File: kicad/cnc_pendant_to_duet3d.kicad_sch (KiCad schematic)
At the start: 9 parts, among them J1 Conn_01x04_Male, J2 DA15_Socket_MountingHoles, U1 Sparkfun_Pro_Micro

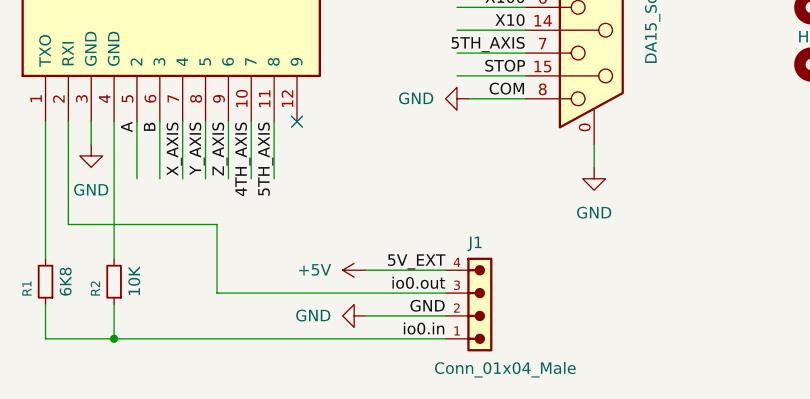
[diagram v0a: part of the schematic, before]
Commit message: Confusion over connecting to Duet and PanelDue
Change to silkscreens
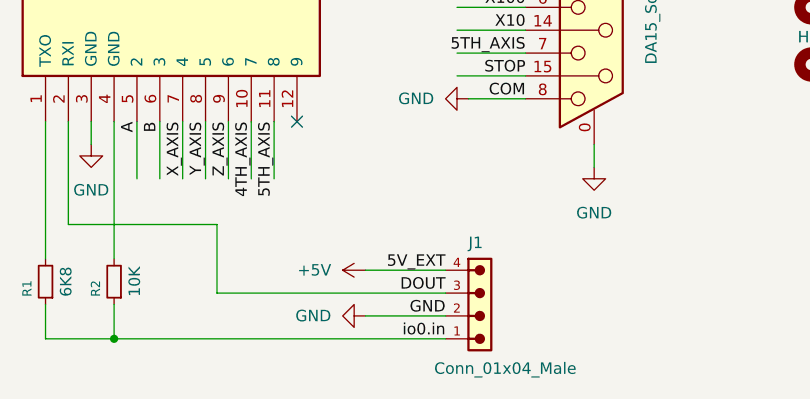
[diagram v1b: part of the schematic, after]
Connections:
- net io0.out renamed DOUT
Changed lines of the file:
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@@
 		)
 	)
-	(label "io0.out"
+	(label "DOUT"
 		(at 82.55 86.36 180)
 		(effects

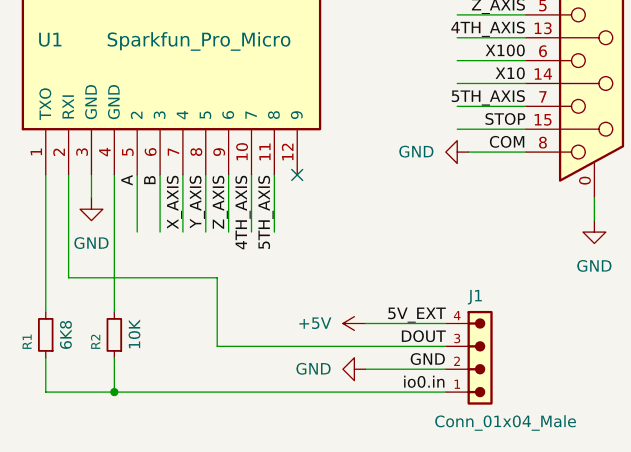
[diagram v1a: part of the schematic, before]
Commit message: 10k resistor and Arduino pin 4 to GND
PCB not updated from schematic at this point
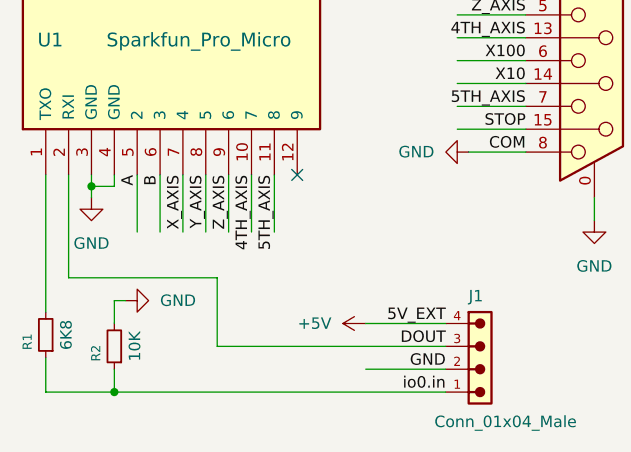
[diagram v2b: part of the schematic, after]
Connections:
- net GND: now also R2.2, U1.4 (GND)
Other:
- moved on the sheet: R2
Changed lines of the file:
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@@
+		(color 0 0 0 0)
+	)
+	(junction
+		(at 43.18 68.58)
+		(diameter 0)
 		(color 0 0 0 0)
 	)
@@
 	(wire
 		(pts
+			(xy 45.72 67.31) (xy 45.72 68.58)
+		)
+		(stroke
+			(width 0)
+			(type default)
+		)
+	)
+	(wire
+		(pts
 			(xy 151.13 54.61) (xy 151.13 57.15)
 		)
@@
 	(wire
 		(pts
+			(xy 45.72 81.28) (xy 46.99 81.28)
+		)
+		(stroke
+			(width 0)
+			(type default)
+		)
+	)
+	(wire
+		(pts
 			(xy 55.88 36.83) (xy 55.88 27.94)
 		)
@@
 	(wire
 		(pts
+			(xy 43.18 68.58) (xy 45.72 68.58)
+		)
+		(stroke
+			(width 0)
+			(type default)
+		)
+	)
+	(wire
+		(pts
 			(xy 82.55 88.9) (xy 73.66 88.9)
 		)
@@
 	(wire
 		(pts
+			(xy 45.72 83.82) (xy 45.72 81.28)
+		)
+		(stroke
+			(width 0)
+			(type default)
+		)
+	)
+	(wire
+		(pts
 			(xy 73.66 83.82) (xy 82.55 83.82)
 		)
@@
 	(wire
 		(pts
-			(xy 45.72 87.63) (xy 45.72 91.44)
+			(xy 45.72 88.9) (xy 45.72 91.44)
 		)
 		(stroke
@@
 	(wire
 		(pts
-			(xy 43.18 67.31) (xy 43.18 69.85)
+			(xy 43.18 67.31) (xy 43.18 68.58)
 		)
 		(stroke
@@
 	(wire
 		(pts
+			(xy 43.18 68.58) (xy 43.18 69.85)
+		)
+		(stroke
+			(width 0)
+			(type default)
+		)
+	)
+	(wire
+		(pts
 			(xy 91.44 34.29) (xy 83.82 34.29)
 		)
@@
 		(pts
 			(xy 83.82 39.37) (xy 91.44 39.37)
-		)
-		(stroke
-			(width 0)
-			(type default)
-		)
-	)
-	(wire
-		(pts
-			(xy 45.72 67.31) (xy 45.72 82.55)
 		)
 		(stroke
@@
 	(symbol
 		(lib_id "Device:R_Small")
-		(at 45.72 85.09 180)
+		(at 45.72 86.36 180)
 		(unit 1)
 		(exclude_from_sim no)
@@
 		(dnp no)
 		(property "Reference" "R2"
-			(at 43.688 85.852 90)
+			(at 43.688 87.122 90)
 			(effects
 				(font
@@
 		)
 		(property "Value" "10K"
-			(at 48.006 85.09 90)
+			(at 48.006 86.36 90)
 			(effects
 				(font
@@
 		)
 		(property "Footprint" "Resistor_SMD:R_1206_3216Metric_Pad1.30x1.75mm_HandSolder"
-			(at 45.72 85.09 0)
+			(at 45.72 86.36 0)
 			(effects
 				(font
@@
 		)
 		(property "Datasheet" "~"
-			(at 45.72 85.09 0)
+			(at 45.72 86.36 0)
 			(effects
 				(font
@@
 		)
 		(property "Description" "Resistor, small symbol"
-			(at 45.72 85.09 0)
+			(at 45.72 86.36 0)
 			(effects
 				(font
@@
 	(symbol
 		(lib_id "power:GND")
-		(at 73.66 88.9 270)
+		(at 46.99 81.28 90)
 		(unit 1)
 		(exclude_from_sim no)
@@
 		(fields_autoplaced yes)
 		(property "Reference" "#PWR010"
-			(at 67.31 88.9 0)
+			(at 53.34 81.28 0)
 			(effects
 				(font
@@
 		)
 		(property "Value" "GND"
-			(at 69.85 88.8999 90)
+			(at 50.8 81.2799 90)
 			(effects
 				(font
@@
 		)
 		(property "Footprint" ""
-			(at 73.66 88.9 0)
+			(at 46.99 81.28 0)
 			(effects
 				(font
@@
 		)
 		(property "Datasheet" ""
-			(at 73.66 88.9 0)
+			(at 46.99 81.28 0)
 			(effects
 				(font
@@
 		)
 		(property "Description" "Power symbol creates a global label with name \"GND\" , ground"
-			(at 73.66 88.9 0)
+			(at 46.99 81.28 0)
 			(effects
 				(font
@@
 		)
 		(instances
-			(project "Duet3D CNC Pendant THT"
+			(project "cnc_pendant_to_duet3d"
 				(path "/f1ac55ef-01a2-453a-a0a9-d83e81c0bdc4"
 					(reference "#PWR010")

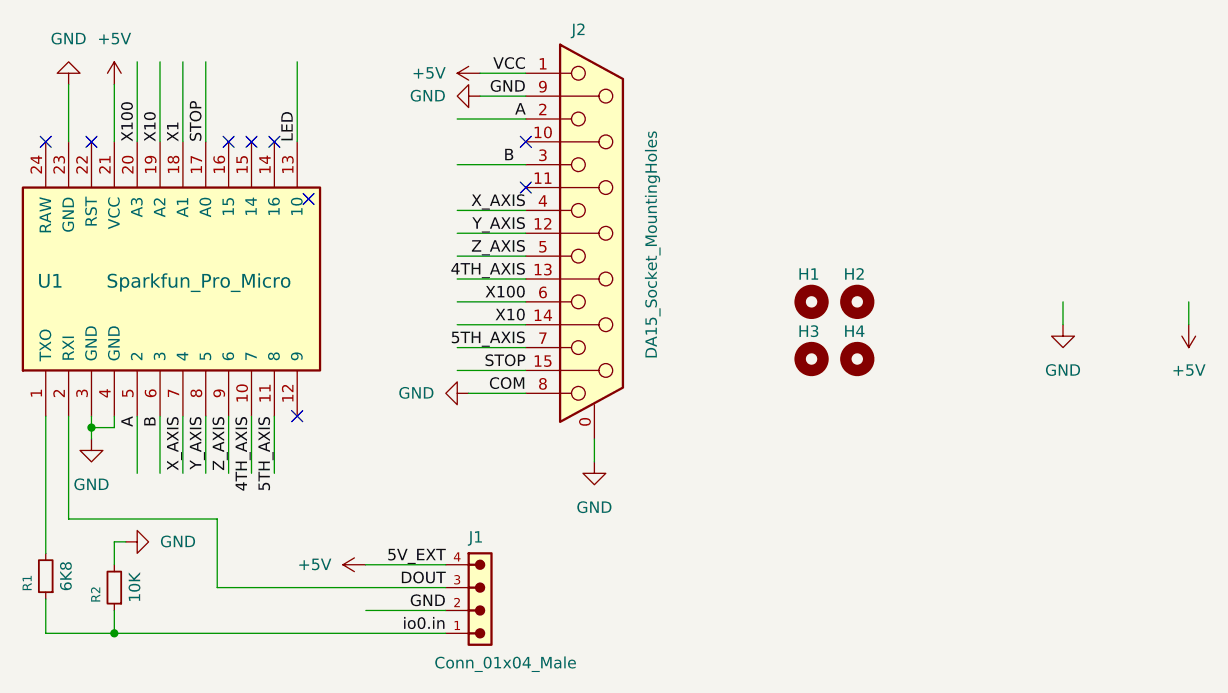
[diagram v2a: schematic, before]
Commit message: Switched to global labels in schematic. Updated PCB
Not tested
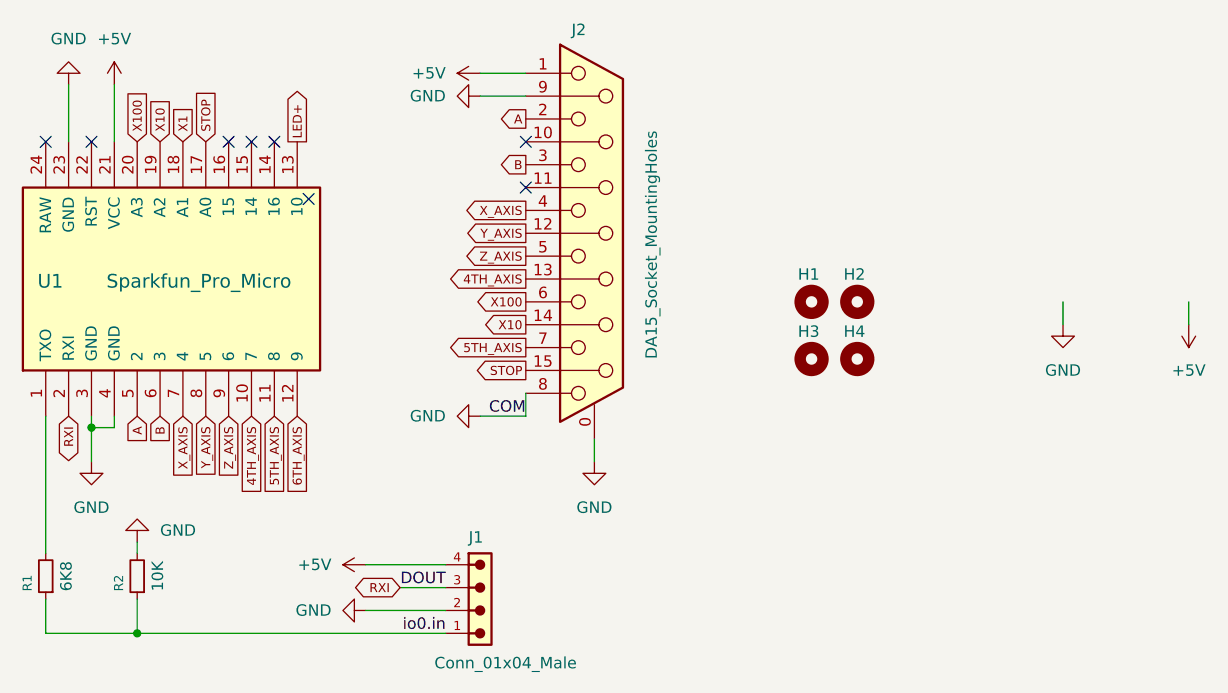
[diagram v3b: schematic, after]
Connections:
- net 6TH_AXIS: now reaches U1.12 (9)
- net DOUT renamed RXI
- net LED renamed LED+
- no-connect marks 9 -> 8
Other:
- moved on the sheet: R2
